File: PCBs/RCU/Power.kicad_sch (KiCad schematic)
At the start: 36 parts, among them J100 Conn_01x02, U100 AP63203WU, U102 AZ1117-3.3, U103 AP63203WU, U104 LM2576S-ADJ

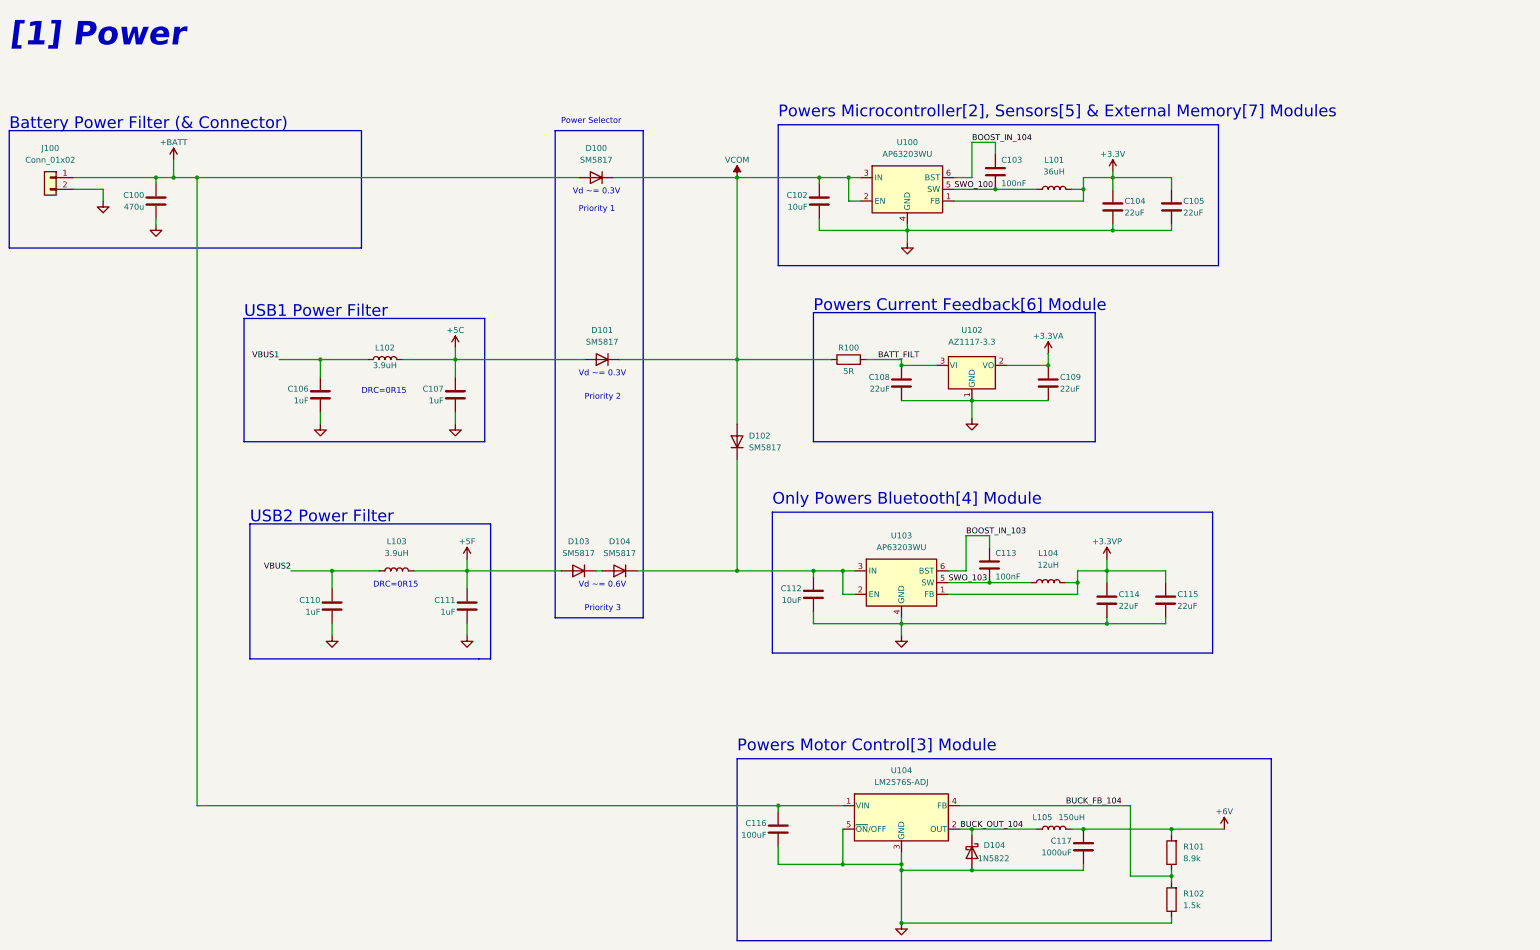
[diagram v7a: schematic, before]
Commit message: Add footrpints to TVS diodes in [3]
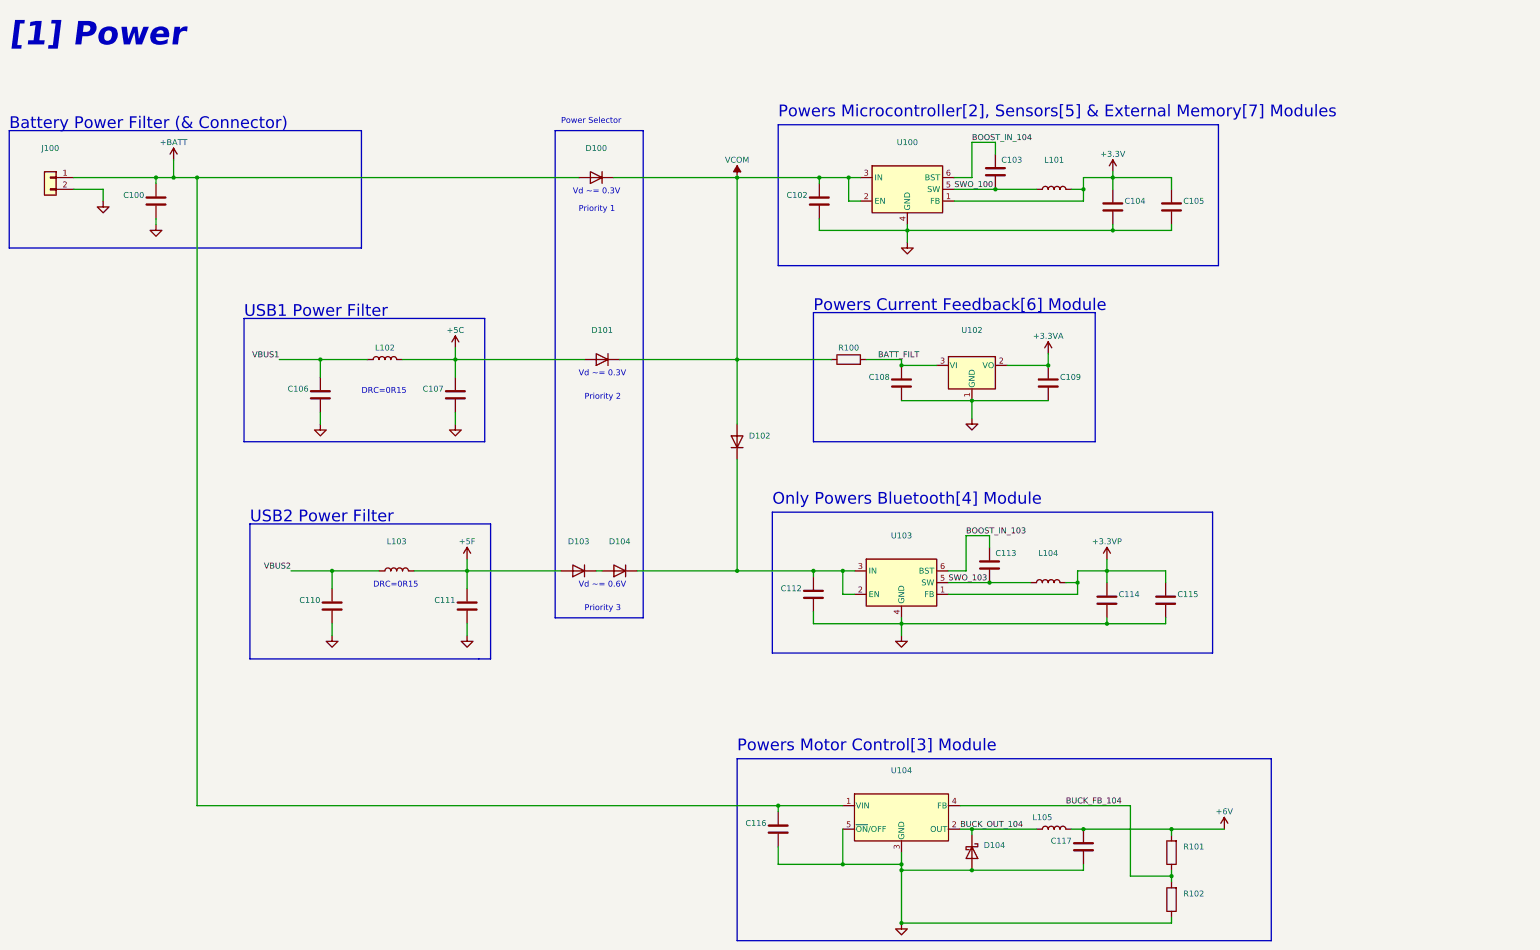
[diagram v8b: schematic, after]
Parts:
- C100: value 470u -> (none)
- C102, C112: value 10uF -> (none)
- C103, C113: value 100nF -> (none)
- C104, C105, C108, C109, C114, C115: value 22uF -> (none)
- C106, C107, C110, C111: value 1uF -> (none)
- C116: value 100uF -> (none)
- C117: value 1000uF -> (none)
- D100, D101, D102, D103, D104: value SM5817 -> (none); footprint Schottky_Diode:SODFL3719X135N -> (none)
- D104: value 1N5822 -> (none); footprint Diode_THT:D_DO-201AD_P15.24mm_Horizontal -> (none)
- J100: value Conn_01x02 -> (none); footprint Connector_Wire:SolderWire-2sqmm_1x02_P7.8mm_D2mm_OD3.9mm -> (none)
- L101: value 36uH -> (none)
- L102, L103: value 3.9uH -> (none)
- L104: value 12uH -> (none)
- L105: value 150uH -> (none)
- R100: value 5R -> (none)
- R101: value 8.9k -> (none)
- R102: value 1.5k -> (none)
- U100, U103: value AP63203WU -> (none); footprint Package_TO_SOT_SMD:TSOT-23-6 -> (none)
- U102: value AZ1117-3.3 -> (none); footprint Package_TO_SOT_SMD:TO-252-2 -> (none)
- U104: value LM2576S-ADJ -> (none); footprint Package_TO_SOT_SMD:TO-263-5_TabPin3 -> (none)
